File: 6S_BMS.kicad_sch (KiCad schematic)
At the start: 46 parts, among them J1 JST_EH_B8B-EH-A, J2 BM06B-GHS-TBT, J3 Conn_ARM_SWD_TagConnect_TC203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, J5 Conn_01x04_Pin, J6 Conn_01x04_Pin, SW1 SW_SPST, U1 BQ76925RGER, U2 STM32L431KCUx, U5 TLV75533PDBV

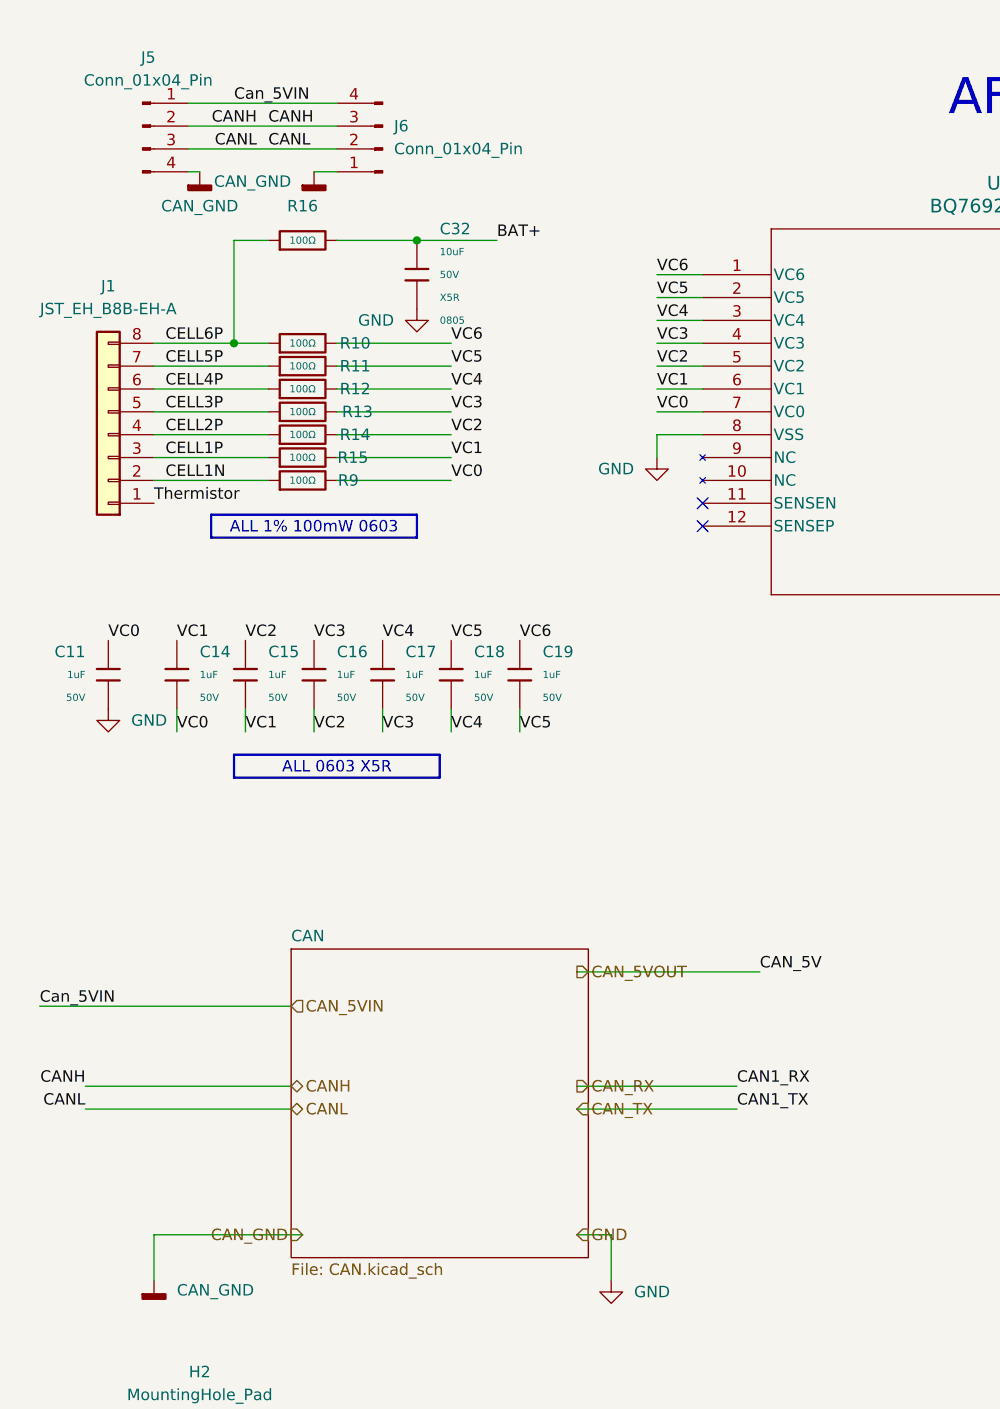
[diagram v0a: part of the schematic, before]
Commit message: Updated Hierarchical Labels
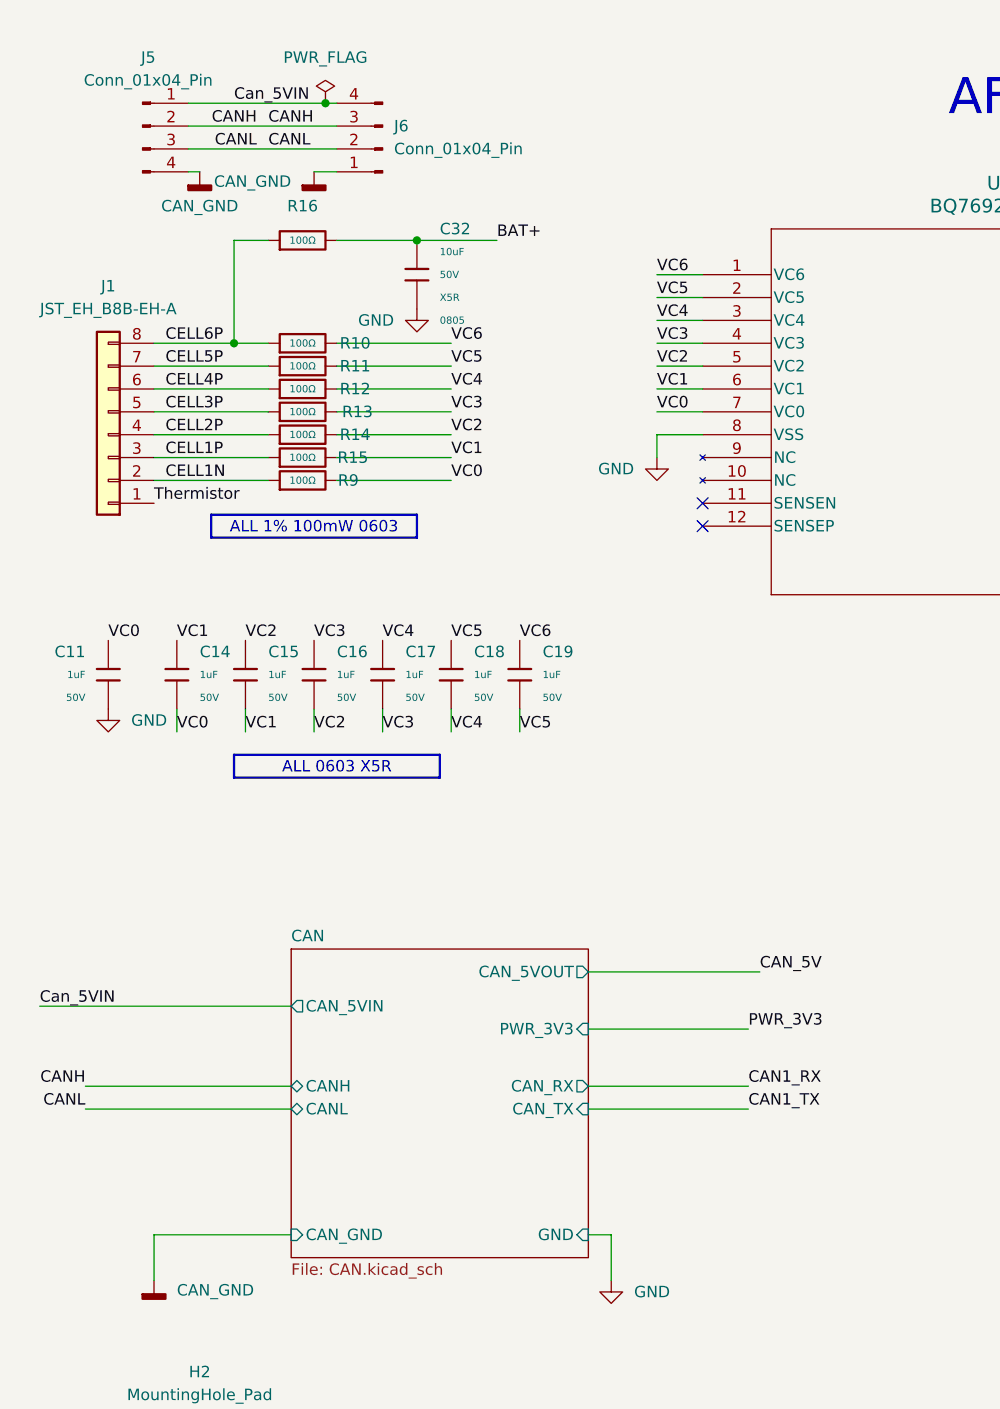
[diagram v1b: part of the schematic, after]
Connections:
- net CAN_5VIN renamed Can_5VIN
- net CAN_RX renamed CAN1_RX
- net CAN_TX renamed CAN1_TX
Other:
- sheet CAN ports: added CANH, CANL, CAN_5VIN, CAN_5VOUT, CAN_GND, CAN_RX, CAN_TX, GND, PWR_3V3; removed none
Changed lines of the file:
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@@
 		(color 0 0 0 0)
 	)
+	(junction
+		(at 46.99 22.86)
+		(diameter 0)
+		(color 0 0 0 0)
+	)
 	(no_connect
 		(at 252.73 49.53)
@@
 	(wire
 		(pts
+			(xy 48.26 38.1) (xy 57.15 38.1)
+		)
+		(stroke
+			(width 0)
+			(type default)
+		)
+	)
+	(wire
+		(pts
 			(xy 229.87 91.44) (xy 229.87 92.71)
 		)
@@
 	(wire
 		(pts
+			(xy 76.2 119.38) (xy 95.25 119.38)
+		)
+		(stroke
+			(width 0)
+			(type default)
+		)
+	)
+	(wire
+		(pts
 			(xy 48.26 59.69) (xy 60.96 59.69)
 		)
@@
 	(wire
 		(pts
-			(xy 74.93 148.59) (xy 78.74 148.59)
+			(xy 76.2 148.59) (xy 78.74 148.59)
 		)
 		(stroke
@@
 	(wire
 		(pts
-			(xy 154.94 54.61) (xy 182.88 54.61)
+			(xy 27.94 148.59) (xy 27.94 153.67)
 		)
 		(stroke
@@
 	(wire
 		(pts
-			(xy 229.87 102.87) (xy 229.87 100.33)
+			(xy 154.94 54.61) (xy 182.88 54.61)
 		)
 		(stroke
@@
 	(wire
 		(pts
-			(xy 48.26 38.1) (xy 57.15 38.1)
+			(xy 229.87 102.87) (xy 229.87 100.33)
 		)
 		(stroke
@@
 	(wire
 		(pts
-			(xy 31.75 22.86) (xy 48.26 22.86)
+			(xy 31.75 22.86) (xy 46.99 22.86)
 		)
 		(stroke
@@
 	(wire
 		(pts
-			(xy 31.75 25.4) (xy 48.26 25.4)
+			(xy 93.98 125.73) (xy 76.2 125.73)
 		)
 		(stroke
@@
 	(wire
 		(pts
-			(xy 215.9 41.91) (xy 215.9 45.72)
+			(xy 31.75 25.4) (xy 48.26 25.4)
 		)
 		(stroke
@@
 	(wire
 		(pts
-			(xy 204.47 36.83) (xy 227.33 36.83)
+			(xy 215.9 41.91) (xy 215.9 45.72)
 		)
 		(stroke
@@
 	(wire
 		(pts
-			(xy 27.94 148.59) (xy 27.94 153.67)
+			(xy 204.47 36.83) (xy 227.33 36.83)
 		)
 		(stroke
@@
 	(wire
 		(pts
+			(xy 46.99 22.86) (xy 48.26 22.86)
+		)
+		(stroke
+			(width 0)
+			(type default)
+		)
+	)
+	(wire
+		(pts
 			(xy 129.54 133.35) (xy 138.43 133.35)
 		)
@@
 	(wire
 		(pts
-			(xy 44.45 148.59) (xy 27.94 148.59)
+			(xy 43.18 148.59) (xy 27.94 148.59)
 		)
 		(stroke
@@
 	(wire
 		(pts
-			(xy 74.93 134.62) (xy 92.71 134.62)
+			(xy 76.2 134.62) (xy 93.98 134.62)
 		)
 		(stroke
@@
 	(wire
 		(pts
-			(xy 74.93 132.08) (xy 92.71 132.08)
+			(xy 76.2 132.08) (xy 93.98 132.08)
 		)
 		(stroke
@@
 	(wire
 		(pts
-			(xy 74.93 119.38) (xy 95.25 119.38)
-		)
-		(stroke
-			(width 0)
-			(type default)
-		)
-	)
-	(wire
-		(pts
 			(xy 36.83 49.53) (xy 36.83 38.1)
 		)
@@
 	)
 	(label "CAN1_TX"
-		(at 92.71 134.62 0)
+		(at 93.98 134.62 0)
 		(effects
 			(font
@@
 		)
 	)
+	(label "PWR_3V3"
+		(at 93.98 125.73 0)
+		(effects
+			(font
+				(size 1.27 1.27)
+			)
+			(justify left bottom)
+		)
+	)
 	(label "CANL"
 		(at 20.32 134.62 180)
@@
 	)
 	(label "CAN1_RX"
-		(at 92.71 132.08 0)
+		(at 93.98 132.08 0)
 		(effects
 			(font
@@
 		)
 	)
-	(hierarchical_label "CAN_TX"
-		(shape input)
-		(at 74.93 134.62 0)
-		(effects
-			(font
-				(size 1.27 1.27)
-			)
-			(justify left)
-		)
-	)
-	(hierarchical_label "CAN_5VIN"
-		(shape input)
-		(at 43.18 123.19 0)
-		(effects
-			(font
-				(size 1.27 1.27)
-			)
-			(justify left)
-		)
-	)
-	(hierarchical_label "CAN_GND"
-		(shape input)
-		(at 44.45 148.59 180)
-		(effects
-			(font
-				(size 1.27 1.27)
-			)
-			(justify right)
-		)
-	)
-	(hierarchical_label "CAN_RX"
-		(shape output)
-		(at 74.93 132.08 0)
-		(effects
-			(font
-				(size 1.27 1.27)
-			)
-			(justify left)
-		)
-	)
-	(hierarchical_label "CANH"
-		(shape bidirectional)
-		(at 43.18 132.08 0)
-		(effects
-			(font
-				(size 1.27 1.27)
-			)
-			(justify left)
-		)
-	)
-	(hierarchical_label "CANL"
-		(shape bidirectional)
-		(at 43.18 134.62 0)
-		(effects
-			(font
-				(size 1.27 1.27)
-			)
-			(justify left)
-		)
-	)
-	(hierarchical_label "GND"
-		(shape input)
-		(at 74.93 148.59 0)
-		(effects
-			(font
-				(size 1.27 1.27)
-			)
-			(justify left)
-		)
-	)
-	(hierarchical_label "CAN_5VOUT"
-		(shape output)
-		(at 74.93 119.38 0)
-		(effects
-			(font
-				(size 1.27 1.27)
-			)
-			(justify left)
-		)
-	)
 	(symbol
 		(lib_id "power:GND")
@@
 	)
 	(symbol
+		(lib_id "power:PWR_FLAG")
+		(at 46.99 22.86 0)
+		(unit 1)
+		(exclude_from_sim no)
+		(in_bom yes)
+		(on_board yes)
+		(dnp no)
+		(fields_autoplaced yes)
+		(property "Reference" "#FLG01"
+			(at 46.99 20.955 0)
+			(effects
+				(font
+					(size 1.27 1.27)
+				)
+				(hide yes)
+			)
+		)
+		(property "Value" "PWR_FLAG"
+			(at 46.99 17.78 0)
+			(effects
+				(font
+					(size 1.27 1.27)
+				)
+			)
+		)
+		(property "Footprint" ""
+			(at 46.99 22.86 0)
+			(effects
+				(font
+					(size 1.27 1.27)
+				)
+				(hide yes)
+			)
+		)
+		(property "Datasheet" "~"
+			(at 46.99 22.86 0)
+			(effects
+				(font
+					(size 1.27 1.27)
+				)
+				(hide yes)
+			)
+		)
+		(property "Description" "Special symbol for telling ERC where power comes from"
+			(at 46.99 22.86 0)
+			(effects
+				(font
+					(size 1.27 1.27)
+				)
+				(hide yes)
+			)
+		)
+		(pin "1"
+		)
+		(instances
+			(project ""
+				(path "/22235745-c803-43e1-a7e4-b86ded892fce"
+					(reference "#FLG01")
+					(unit 1)
+				)
+			)
+		)
+	)
+	(symbol
 		(lib_id "PCM_JLCPCB-Capacitors:0603,100nF")
 		(at 219.71 27.94 180)
@@
 			)
 		)
+		(pin "CANH" bidirectional
+			(at 43.18 132.08 180)
+			(effects
+				(font
+					(size 1.27 1.27)
+				)
+				(justify left)
+			)
+		)
+		(pin "CANL" bidirectional
+			(at 43.18 134.62 180)
+			(effects
+				(font
+					(size 1.27 1.27)
+				)
+				(justify left)
+			)
+		)
+		(pin "CAN_5VIN" output
+			(at 43.18 123.19 180)
+			(effects
+				(font
+					(size 1.27 1.27)
+				)
+				(justify left)
+			)
+		)
+		(pin "CAN_5VOUT" output
+			(at 76.2 119.38 0)
+			(effects
+				(font
+					(size 1.27 1.27)
+				)
+				(justify right)
+			)
+		)
+		(pin "CAN_GND" input
+			(at 43.18 148.59 180)
+			(effects
+				(font
+					(size 1.27 1.27)
+				)
+				(justify left)
+			)
+		)
+		(pin "CAN_RX" output
+			(at 76.2 132.08 0)
+			(effects
+				(font
+					(size 1.27 1.27)
+				)
+				(justify right)
+			)
+		)
+		(pin "CAN_TX" input
+			(at 76.2 134.62 0)
+			(effects
+				(font
+					(size 1.27 1.27)
+				)
+				(justify right)
+			)
+		)
+		(pin "GND" input
+			(at 76.2 148.59 0)
+			(effects
+				(font
+					(size 1.27 1.27)
+				)
+				(justify right)
+			)
+		)
+		(pin "PWR_3V3" input
+			(at 76.2 125.73 0)
+			(effects
+				(font
+					(size 1.27 1.27)
+				)
+				(justify right)
+			)
+		)

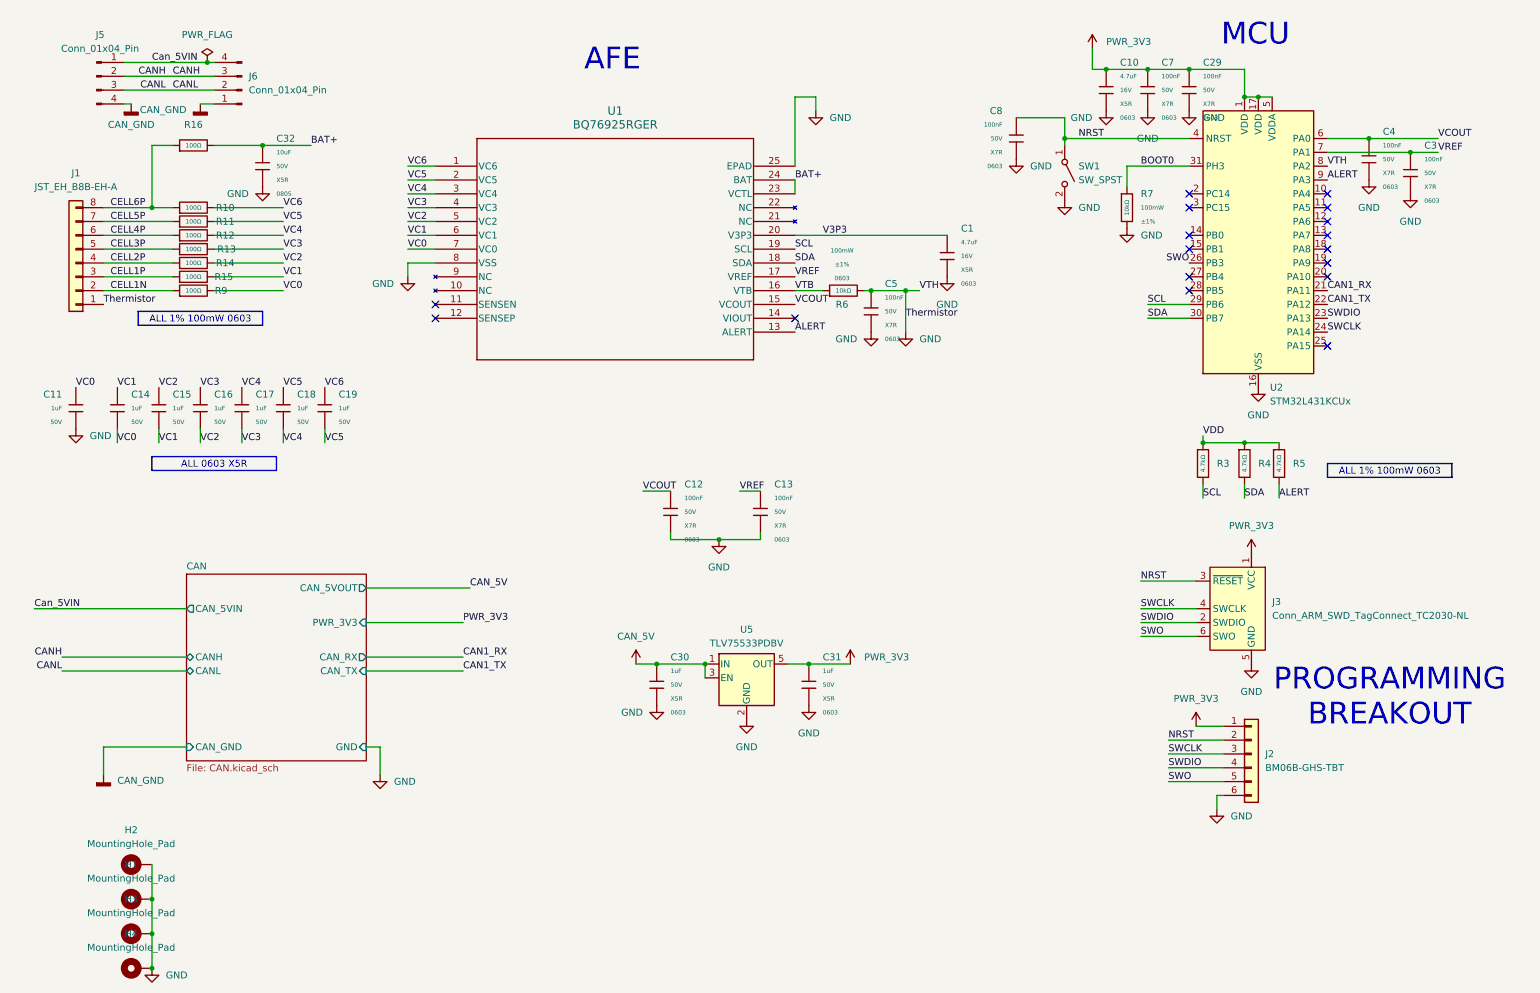
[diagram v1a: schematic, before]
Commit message: Fixed ERC errors and updated schem layout
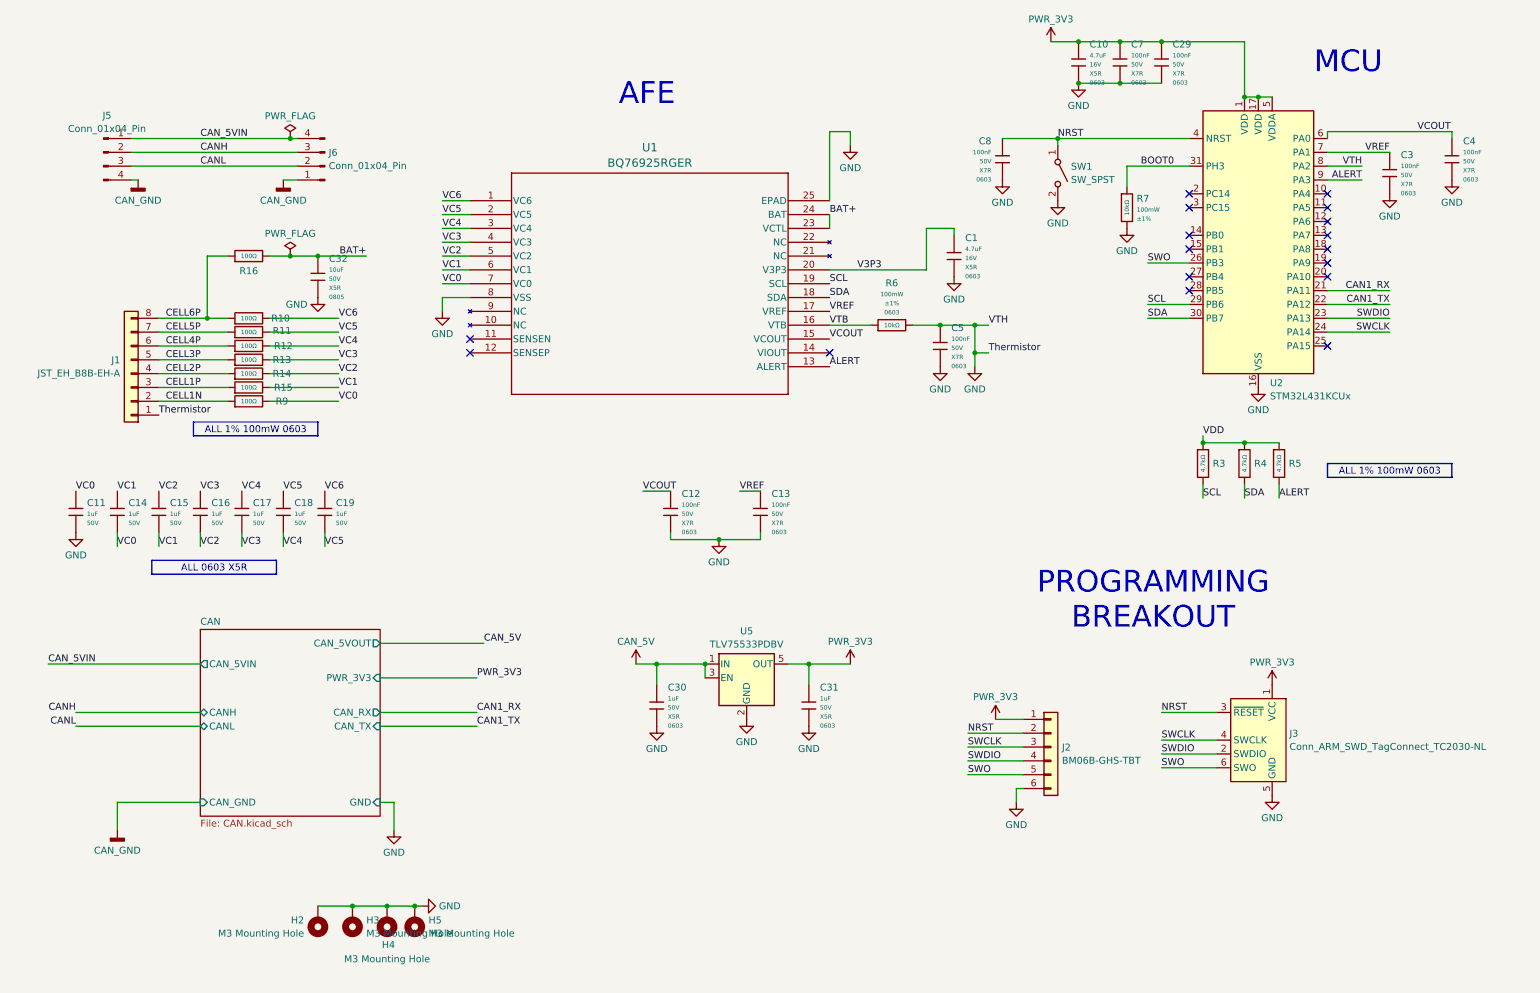
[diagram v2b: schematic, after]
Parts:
- removed H1: MountingHole_Pad, MountingHole:MountingHole_3.2mm_M3_Pad, symbol Mechanical:MountingHole_Pad
- added H5: M3 Mounting Hole, MountingHole:MountingHole_3.2mm_M3_Pad, symbol Mechanical:MountingHole_Pad
- H2, H3, H4: value MountingHole_Pad -> M3 Mounting Hole
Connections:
- net GND: now also H5.1
- net Can_5VIN renamed CAN_5VIN
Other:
- moved on the sheet: C1, C10, C11, C14, C15, C16, C17, C18, C19, C29, C3, C30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
